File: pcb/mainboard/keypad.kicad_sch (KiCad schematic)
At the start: 20 parts, among them Y100 Crystal

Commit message: - pcb: working on r0p1 sch
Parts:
- removed ARM_JTAG1: Conn_02x05_Odd_Even, Connector_PinHeader_1.27mm:PinHeader_2x05_P1.27mm_Vertical_SMD, symbol Connector_Generic:Conn_02x05_Odd_Even
- removed C112, C113: 470nF, Capacitor_SMD:C_0402_1005Metric, symbol Device:C
- removed C114: 4.7uF, Capacitor_SMD:C_0603_1608Metric, symbol Device:C
- removed C115, C116: 18pF, Capacitor_SMD:C_0402_1005Metric, symbol Device:C
- removed C?: 100nF, symbol Device:C
- removed D100, D101: 1N5819, Diode_SMD:D_SOD-123, symbol Device:D_Schottky
- removed FB?: Ferrite_Bead, symbol Device:Ferrite_Bead
- removed J?: Conn_01x24_MountingPin, symbol Connector_Generic_MountingPin:Conn_01x24_MountingPin
- removed J?: Conn_01x12_MountingPin, symbol Connector_Generic_MountingPin:Conn_01x12_MountingPin
- removed R109: 2.2M, Capacitor_SMD:C_0402_1005Metric, symbol Device:R
- removed R110, R111, R118: 10K, Capacitor_SMD:C_0402_1005Metric, symbol Device:R
- removed R114, R115: 22R, Capacitor_SMD:C_0402_1005Metric, symbol Device:R
- removed U?: GD32VF103C8Tx, Package_QFP:LQFP-48_7x7mm_P0.5mm, symbol MCU_ST_STM32F1:STM32F103C8Tx
- removed Y100: Crystal, Crystal:Crystal_SMD_TXC_9HT11-2Pin_2.0x1.2mm_HandSoldering, symbol Device:Crystal
- added J?: Conn_01x28_MountingPin, symbol Connector_Generic_MountingPin:Conn_01x28_MountingPin
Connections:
- net GND: now also J?.28 (Pin_28), J?.MP (MountPin)
- new net KBD_DET: J?.27 (Pin_27)
- new net KSI0: J?.2 (Pin_2)
- new net KSI1: J?.5 (Pin_5)
- new net KSI2: J?.7 (Pin_7)
- new net KSI3: J?.9 (Pin_9)
- new net KSI4: J?.11 (Pin_11)
- new net KSI5: J?.12 (Pin_12)
- new net KSI6: J?.14 (Pin_14)
- new net KSI7: J?.15 (Pin_15)
- new net KSO0: J?.1 (Pin_1)
- new net KSO1: J?.22 (Pin_22), J?.3 (Pin_3)
- new net KSO10: J?.19 (Pin_19)
- new net KSO11: J?.20 (Pin_20)
- new net KSO12: J?.21 (Pin_21)
- new net KSO13: J?.23 (Pin_23)
- new net KSO14: J?.24 (Pin_24)
- new net KSO15: J?.26 (Pin_26)
- new net KSO2: J?.4 (Pin_4)
- new net KSO3: J?.25 (Pin_25), J?.6 (Pin_6)
- new net KSO4: J?.8 (Pin_8)
- new net KSO5: J?.10 (Pin_10)
- new net KSO6: J?.13 (Pin_13)
- new net KSO7: J?.16 (Pin_16)
- new net KSO8: J?.17 (Pin_17)
- new net KSO9: J?.18 (Pin_18)
- no-connect marks 9 -> 0

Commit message: - pcb: r0p1 sch draft
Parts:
- gave numbers to parts that had none: 1
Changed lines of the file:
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@@
 (kicad_sch (version 20210406) (generator eeschema)
-  (paper "A4")
+  (paper "A3")
   (title_block
     (title "Archer")
@@
   (symbol (lib_id "Connector_Generic_MountingPin:Conn_01x28_MountingPin") (at 160.02 96.52 0) (unit 1)
     (in_bom yes) (on_board yes) (fields_autoplaced)
-    (property "Reference" "J?" (id 0) (at 162.56 99.1869 0)
+    (property "Reference" "J800" (id 0) (at 162.56 99.1869 0)
       (effects (font (size 1.27 1.27)) (justify left))
     )

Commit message: - pcb: start r0p1 layout
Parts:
- J800: footprint (none) -> Connector_FFC-FPC:Molex_200528-0280_1x28-1MP_P1.00mm_Horizontal
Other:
- company: Copyright EI-2030 2021. -> Copyright EI-2030 2021. / Engineer: Wenting Zhang
- title: Archer -> Archer Mainboard
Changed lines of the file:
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@@
   (paper "A3")
   (title_block
-    (title "Archer")
-    (date "2021-04-26")
+    (title "Archer Mainboard")
+    (date "2021-05-05")
     (rev "R0.1 draft")
-    (company "Copyright EI-2030 2021.")
+    (company "Copyright EI-2030 2021. / Engineer: Wenting Zhang")
     (comment 2 "MERCHANTABILITY, SATISFACTORY QUALITY AND FITNESS FOR A PARTICULAR PURPOSE.")
-    (comment 3 "source is distributed WITHOUT ANY EXPRESS OR IMPLIED WARRANTY, INCLUDING OF")
-    (comment 4 "This source describes Open Hardware and is licensed under the CERN-OHL-S v2. This ")
+    (comment 3 "This source is distributed WITHOUT ANY EXPRESS OR IMPLIED WARRANTY, INCLUDING OF")
+    (comment 4 "This source describes Open Hardware and is licensed under the CERN-OHL-S v2.")
   )
   (junction (at 149.86 68.58) (diameter 0.9144) (color 0 0 0 0))
@@
     (stroke (width 0) (type solid) (color 0 0 0 0))
   )
-  (global_label "KSO0" (shape output) (at 147.32 63.5 180) (fields_autoplaced)
+  (global_label "KSO0" (shape input) (at 147.32 63.5 180) (fields_autoplaced)
     (effects (font (size 1.27 1.27)) (justify right))
     (property "Intersheet References" "${INTERSHEET_REFS}" (id 0) (at 139.8874 63.4206 0)
@@
     )
   )
-  (global_label "KSI0" (shape input) (at 147.32 66.04 180) (fields_autoplaced)
+  (global_label "KSI0" (shape output) (at 147.32 66.04 180) (fields_autoplaced)
     (effects (font (size 1.27 1.27)) (justify right))
     (property "Intersheet References" "${INTERSHEET_REFS}" (id 0) (at 140.6131 65.9606 0)
@@
     )
   )
-  (global_label "KSO1" (shape output) (at 147.32 68.58 180) (fields_autoplaced)
+  (global_label "KSO1" (shape input) (at 147.32 68.58 180) (fields_autoplaced)
     (effects (font (size 1.27 1.27)) (justify right))
     (property "Intersheet References" "${INTERSHEET_REFS}" (id 0) (at 139.8874 68.5006 0)
@@
     )
   )
-  (global_label "KSO2" (shape output) (at 147.32 71.12 180) (fields_autoplaced)
+  (global_label "KSO2" (shape input) (at 147.32 71.12 180) (fields_autoplaced)
     (effects (font (size 1.27 1.27)) (justify right))
     (property "Intersheet References" "${INTERSHEET_REFS}" (id 0) (at 139.8874 71.0406 0)
@@
     )
   )
-  (global_label "KSI1" (shape input) (at 147.32 73.66 180) (fields_autoplaced)
+  (global_label "KSI1" (shape output) (at 147.32 73.66 180) (fields_autoplaced)
     (effects (font (size 1.27 1.27)) (justify right))
     (property "Intersheet References" "${INTERSHEET_REFS}" (id 0) (at 140.6131 73.5806 0)
@@
     )
   )
-  (global_label "KSO3" (shape output) (at 147.32 76.2 180) (fields_autoplaced)
+  (global_label "KSO3" (shape input) (at 147.32 76.2 180) (fields_autoplaced)
     (effects (font (size 1.27 1.27)) (justify right))
     (property "Intersheet References" "${INTERSHEET_REFS}" (id 0) (at 139.8874 76.1206 0)
@@
     )
   )
-  (global_label "KSI2" (shape input) (at 147.32 78.74 180) (fields_autoplaced)
+  (global_label "KSI2" (shape output) (at 147.32 78.74 180) (fields_autoplaced)
     (effects (font (size 1.27 1.27)) (justify right))
     (property "Intersheet References" "${INTERSHEET_REFS}" (id 0) (at 140.6131 78.6606 0)
@@
     )
   )
-  (global_label "KSO4" (shape output) (at 147.32 81.28 180) (fields_autoplaced)
+  (global_label "KSO4" (shape input) (at 147.32 81.28 180) (fields_autoplaced)
     (effects (font (size 1.27 1.27)) (justify right))
     (property "Intersheet References" "${INTERSHEET_REFS}" (id 0) (at 139.8874 81.2006 0)
@@
     )
   )
-  (global_label "KSI3" (shape input) (at 147.32 83.82 180) (fields_autoplaced)
+  (global_label "KSI3" (shape output) (at 147.32 83.82 180) (fields_autoplaced)
     (effects (font (size 1.27 1.27)) (justify right))
     (property "Intersheet References" "${INTERSHEET_REFS}" (id 0) (at 140.6131 83.7406 0)
@@
     )
   )
-  (global_label "KSO5" (shape output) (at 147.32 86.36 180) (fields_autoplaced)
+  (global_label "KSO5" (shape input) (at 147.32 86.36 180) (fields_autoplaced)
     (effects (font (size 1.27 1.27)) (justify right))
     (property "Intersheet References" "${INTERSHEET_REFS}" (id 0) (at 139.8874 86.2806 0)
@@
     )
   )
-  (global_label "KSI4" (shape input) (at 147.32 88.9 180) (fields_autoplaced)
+  (global_label "KSI4" (shape output) (at 147.32 88.9 180) (fields_autoplaced)
     (effects (font (size 1.27 1.27)) (justify right))
     (property "Intersheet References" "${INTERSHEET_REFS}" (id 0) (at 140.6131 88.8206 0)
@@
     )
   )
-  (global_label "KSI5" (shape input) (at 147.32 91.44 180) (fields_autoplaced)
+  (global_label "KSI5" (shape output) (at 147.32 91.44 180) (fields_autoplaced)
     (effects (font (size 1.27 1.27)) (justify right))
     (property "Intersheet References" "${INTERSHEET_REFS}" (id 0) (at 140.6131 91.3606 0)
@@
     )
   )
-  (global_label "KSO6" (shape output) (at 147.32 93.98 180) (fields_autoplaced)
+  (global_label "KSO6" (shape input) (at 147.32 93.98 180) (fields_autoplaced)
     (effects (font (size 1.27 1.27)) (justify right))
     (property "Intersheet References" "${INTERSHEET_REFS}" (id 0) (at 139.8874 93.9006 0)
@@
     )
   )
-  (global_label "KSI6" (shape input) (at 147.32 96.52 180) (fields_autoplaced)
+  (global_label "KSI6" (shape output) (at 147.32 96.52 180) (fields_autoplaced)
     (effects (font (size 1.27 1.27)) (justify right))
     (property "Intersheet References" "${INTERSHEET_REFS}" (id 0) (at 140.6131 96.4406 0)
@@
     )
   )
-  (global_label "KSI7" (shape input) (at 147.32 99.06 180) (fields_autoplaced)
+  (global_label "KSI7" (shape output) (at 147.32 99.06 180) (fields_autoplaced)
     (effects (font (size 1.27 1.27)) (justify right))
     (property "Intersheet References" "${INTERSHEET_REFS}" (id 0) (at 140.6131 98.9806 0)
@@
     )
   )
-  (global_label "KSO7" (shape output) (at 147.32 101.6 180) (fields_autoplaced)
+  (global_label "KSO7" (shape input) (at 147.32 101.6 180) (fields_autoplaced)
     (effects (font (size 1.27 1.27)) (justify right))
     (property "Intersheet References" "${INTERSHEET_REFS}" (id 0) (at 139.8874 101.5206 0)
@@
     )
   )
-  (global_label "KSO8" (shape output) (at 147.32 104.14 180) (fields_autoplaced)
+  (global_label "KSO8" (shape input) (at 147.32 104.14 180) (fields_autoplaced)
     (effects (font (size 1.27 1.27)) (justify right))
     (property "Intersheet References" "${INTERSHEET_REFS}" (id 0) (at 139.8874 104.0606 0)
@@
     )
   )
-  (global_label "KSO9" (shape output) (at 147.32 106.68 180) (fields_autoplaced)
+  (global_label "KSO9" (shape input) (at 147.32 106.68 180) (fields_autoplaced)
     (effects (font (size 1.27 1.27)) (justify right))
     (property "Intersheet References" "${INTERSHEET_REFS}" (id 0) (at 139.8874 106.6006 0)
@@
     )
   )
-  (global_label "KSO10" (shape output) (at 147.32 109.22 180) (fields_autoplaced)
+  (global_label "KSO10" (shape input) (at 147.32 109.22 180) (fields_autoplaced)
     (effects (font (size 1.27 1.27)) (justify right))
     (property "Intersheet References" "${INTERSHEET_REFS}" (id 0) (at 139.8874 109.1406 0)
@@
     )
   )
-  (global_label "KSO11" (shape output) (at 147.32 111.76 180) (fields_autoplaced)
+  (global_label "KSO11" (shape input) (at 147.32 111.76 180) (fields_autoplaced)
     (effects (font (size 1.27 1.27)) (justify right))
     (property "Intersheet References" "${INTERSHEET_REFS}" (id 0) (at 139.8874 111.6806 0)
@@
     )
   )
-  (global_label "KSO12" (shape output) (at 147.32 114.3 180) (fields_autoplaced)
+  (global_label "KSO12" (shape input) (at 147.32 114.3 180) (fields_autoplaced)
     (effects (font (size 1.27 1.27)) (justify right))
     (property "Intersheet References" "${INTERSHEET_REFS}" (id 0) (at 139.8874 114.2206 0)
@@
     )
   )
-  (global_label "KSO13" (shape output) (at 147.32 119.38 180) (fields_autoplaced)
+  (global_label "KSO13" (shape input) (at 147.32 119.38 180) (fields_autoplaced)
     (effects (font (size 1.27 1.27)) (justify right))
     (property "Intersheet References" "${INTERSHEET_REFS}" (id 0) (at 139.8874 119.3006 0)
@@
     )
   )
-  (global_label "KSO14" (shape output) (at 147.32 121.92 180) (fields_autoplaced)
+  (global_label "KSO14" (shape input) (at 147.32 121.92 180) (fields_autoplaced)
     (effects (font (size 1.27 1.27)) (justify right))
     (property "Intersheet References" "${INTERSHEET_REFS}" (id 0) (at 139.8874 121.8406 0)
@@
     )
   )
-  (global_label "KSO15" (shape output) (at 147.32 127 180) (fields_autoplaced)
+  (global_label "KSO15" (shape input) (at 147.32 127 180) (fields_autoplaced)
     (effects (font (size 1.27 1.27)) (justify right))
     (property "Intersheet References" "${INTERSHEET_REFS}" (id 0) (at 139.8874 126.9206 0)
@@
   (symbol (lib_id "power:GND") (at 160.02 139.7 0) (unit 1)
     (in_bom yes) (on_board yes) (fields_autoplaced)
-    (property "Reference" "#PWR?" (id 0) (at 160.02 146.05 0)
+    (property "Reference" "#PWR084" (id 0) (at 160.02 146.05 0)
       (effects (font (size 1.27 1.27)) hide)
     )
@@
       (effects (font (size 1.27 1.27)) (justify left))
     )
-    (property "Footprint" "" (id 2) (at 160.02 96.52 0)
-      (effects (font (size 1.27 1.27)) hide)
-    )
+    (property "Footprint" "Connector_FFC-FPC:Molex_200528-0280_1x28-1MP_P1.00mm_Horizontal" (id 2) (at 160.02 96.52 0)
+      (effects (font (size 1.27 1.27)) hide)
+    )

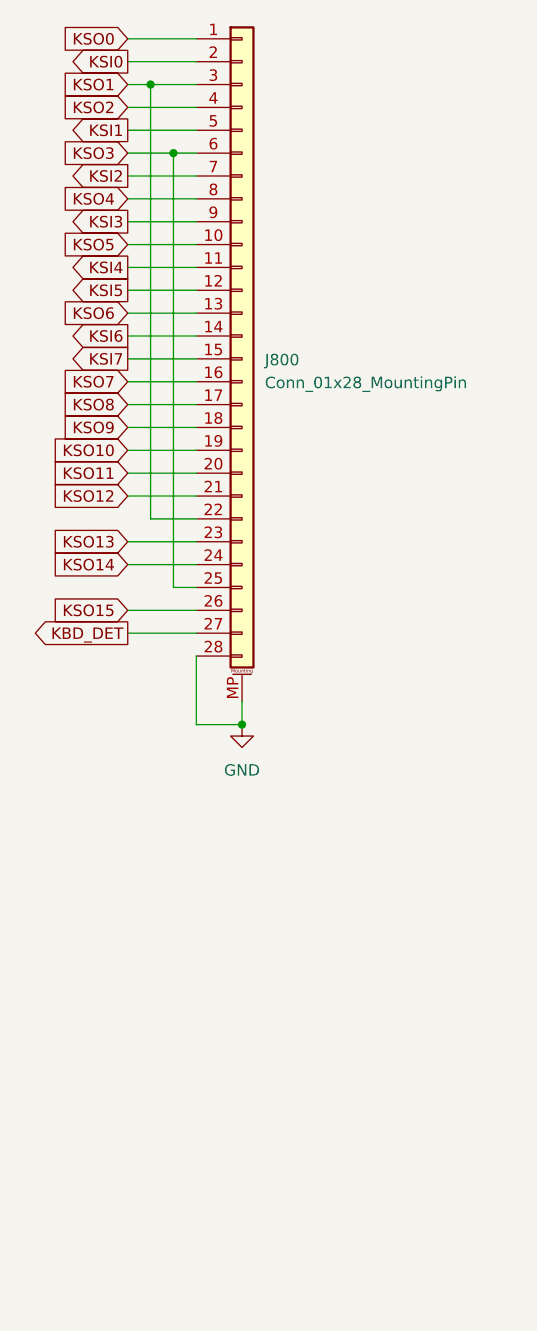
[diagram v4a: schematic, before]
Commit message: - pcb: components placed
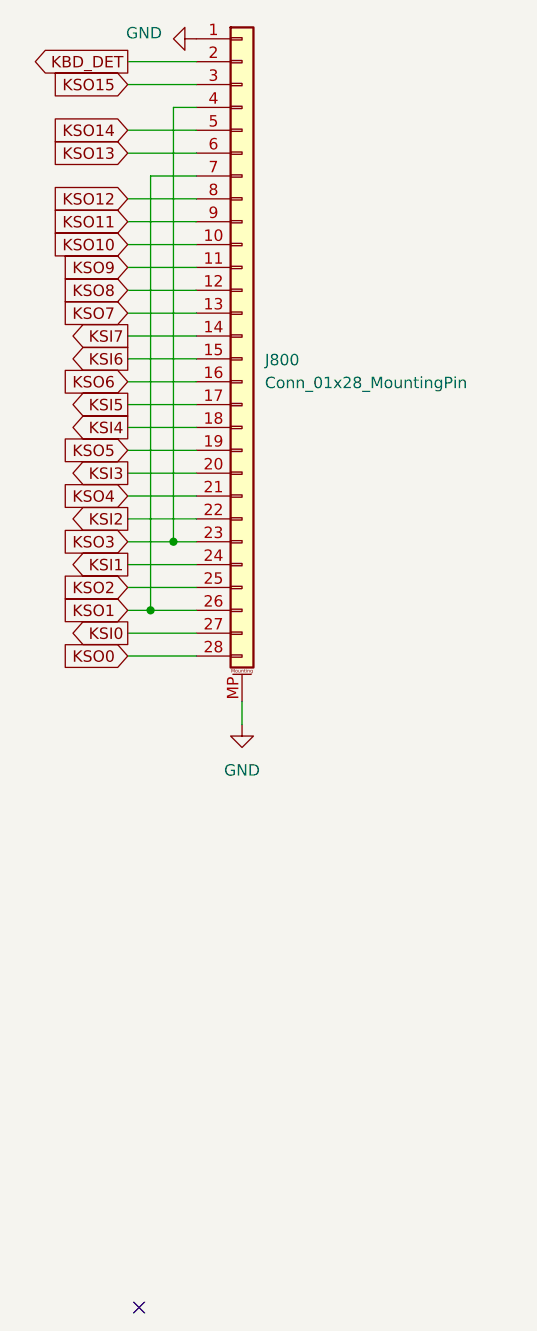
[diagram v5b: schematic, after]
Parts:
- J800: footprint Connector_FFC-FPC:Molex_200528-0280_1x28-1MP_P1.00mm_Horizontal -> Connector_FFC-FPC:TE_2-84953-8_1x28-1MP_P1.0mm_Horizontal
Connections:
- net GND: now also J800.1 (Pin_1); no longer J800.28 (Pin_28)
- net KBD_DET: now also J800.2 (Pin_2); no longer J800.27 (Pin_27)
- net KSI0: now also J800.27 (Pin_27); no longer J800.2 (Pin_2)
- net KSI1: now also J800.24 (Pin_24); no longer J800.5 (Pin_5)
- net KSI2: now also J800.22 (Pin_22); no longer J800.7 (Pin_7)
- net KSI3: now also J800.20 (Pin_20); no longer J800.9 (Pin_9)
- net KSI4: now also J800.18 (Pin_18); no longer J800.11 (Pin_11)
- net KSI5: now also J800.17 (Pin_17); no longer J800.12 (Pin_12)
- net KSI6: now also J800.15 (Pin_15); no longer J800.14 (Pin_14)
- net KSI7: now also J800.14 (Pin_14); no longer J800.15 (Pin_15)
- net KSO0: now also J800.28 (Pin_28); no longer J800.1 (Pin_1)
- net KSO1: now also J800.26 (Pin_26), J800.7 (Pin_7); no longer J800.22 (Pin_22), J800.3 (Pin_3)
- net KSO10: now also J800.10 (Pin_10); no longer J800.19 (Pin_19)
- net KSO11: now also J800.9 (Pin_9); no longer J800.20 (Pin_20)
- net KSO12: now also J800.8 (Pin_8); no longer J800.21 (Pin_21)
- net KSO13: now also J800.6 (Pin_6); no longer J800.23 (Pin_23)
- net KSO14: now also J800.5 (Pin_5); no longer J800.24 (Pin_24)
- net KSO15: now also J800.3 (Pin_3); no longer J800.26 (Pin_26)
- net KSO2: now also J800.25 (Pin_25); no longer J800.4 (Pin_4)
- net KSO3: now also J800.23 (Pin_23), J800.4 (Pin_4); no longer J800.25 (Pin_25), J800.6 (Pin_6)
- net KSO4: now also J800.21 (Pin_21); no longer J800.8 (Pin_8)
- net KSO5: now also J800.19 (Pin_19); no longer J800.10 (Pin_10)
- net KSO6: now also J800.16 (Pin_16); no longer J800.13 (Pin_13)
- net KSO7: now also J800.13 (Pin_13); no longer J800.16 (Pin_16)
- net KSO8: now also J800.12 (Pin_12); no longer J800.17 (Pin_17)
- net KSO9: now also J800.11 (Pin_11); no longer J800.18 (Pin_18)
- no-connect marks 0 -> 1

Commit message: - pcb: finishing layout r0p1
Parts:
- added C800: 100nF, Capacitor_SMD:C_0402_1005Metric, symbol Device:C
- added R800: 1K, Resistor_SMD:R_0402_1005Metric, symbol Device:R
- added SW800: EVQPUJ02K, Button_Switch_SMD:Panasonic_EVQPUJ_EVQPUA, symbol Switch:SW_Push
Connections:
- net GND: now also C800.1, SW800.2
- new net: R800.1, SW800.1
- new net ONOFF: C800.2, R800.2
- no-connect marks 1 -> 0
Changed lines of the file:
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@@
     (comment 4 "This source describes Open Hardware and is licensed under the CERN-OHL-S v2.")
   )
+  (junction (at 132.08 162.56) (diameter 0.9144) (color 0 0 0 0))
   (junction (at 149.86 127) (diameter 0.9144) (color 0 0 0 0))
   (junction (at 152.4 119.38) (diameter 0.9144) (color 0 0 0 0))
-  (no_connect (at 148.59 204.47))
+  (wire (pts (xy 129.54 162.56) (xy 132.08 162.56))
+    (stroke (width 0) (type solid) (color 0 0 0 0))
+  )
+  (wire (pts (xy 132.08 162.56) (xy 132.08 165.1))
+    (stroke (width 0) (type solid) (color 0 0 0 0))
+  )
+  (wire (pts (xy 132.08 162.56) (xy 134.62 162.56))
+    (stroke (width 0) (type solid) (color 0 0 0 0))
+  )
+  (wire (pts (xy 132.08 172.72) (xy 132.08 175.26))
+    (stroke (width 0) (type solid) (color 0 0 0 0))
+  )
+  (wire (pts (xy 142.24 162.56) (xy 147.32 162.56))
+    (stroke (width 0) (type solid) (color 0 0 0 0))
+  )
   (wire (pts (xy 147.32 66.04) (xy 154.94 66.04))
     (stroke (width 0) (type solid) (color 0 0 0 0))
@@
     (stroke (width 0) (type solid) (color 0 0 0 0))
   )
+  (global_label "ONOFF" (shape output) (at 129.54 162.56 180) (fields_autoplaced)
+    (effects (font (size 1.27 1.27)) (justify right))
+    (property "Intersheet References" "${INTERSHEET_REFS}" (id 0) (at 120.9583 162.4806 0)
+      (effects (font (size 1.27 1.27)) (justify right) hide)
+    )
+  )
   (global_label "KBD_DET" (shape output) (at 147.32 66.04 180) (fields_autoplaced)
     (effects (font (size 1.27 1.27)) (justify right))
@@
       (effects (font (size 1.27 1.27)) (justify right) hide)
     )
+  )
+  (symbol (lib_id "power:GND") (at 132.08 175.26 0) (unit 1)
+    (in_bom yes) (on_board yes) (fields_autoplaced)
+    (property "Reference" "#PWR0165" (id 0) (at 132.08 181.61 0)
+      (effects (font (size 1.27 1.27)) hide)
+    )
+    (property "Value" "GND" (id 1) (at 132.08 180.34 0))
+    (property "Footprint" "" (id 2) (at 132.08 175.26 0)
+      (effects (font (size 1.27 1.27)) hide)
+    )
+    (property "Datasheet" "" (id 3) (at 132.08 175.26 0)
+      (effects (font (size 1.27 1.27)) hide)
+    )
+    (pin "1")
   )
   (symbol (lib_id "power:GND") (at 154.94 63.5 270) (unit 1)
@@
     )
     (property "Datasheet" "" (id 3) (at 154.94 63.5 0)
+      (effects (font (size 1.27 1.27)) hide)
+    )
+    (pin "1")
+  )
+  (symbol (lib_id "power:GND") (at 157.48 162.56 90) (unit 1)
+    (in_bom yes) (on_board yes)
+    (property "Reference" "#PWR0164" (id 0) (at 163.83 162.56 0)
+      (effects (font (size 1.27 1.27)) hide)
+    )
+    (property "Value" "GND" (id 1) (at 163.83 162.56 90))
+    (property "Footprint" "" (id 2) (at 157.48 162.56 0)
+      (effects (font (size 1.27 1.27)) hide)
+    )
+    (property "Datasheet" "" (id 3) (at 157.48 162.56 0)
       (effects (font (size 1.27 1.27)) hide)
     )
@@
     (pin "1")
   )
+  (symbol (lib_id "Device:R") (at 138.43 162.56 270) (unit 1)
+    (in_bom yes) (on_board yes)
+    (property "Reference" "R800" (id 0) (at 133.35 161.29 90))
+    (property "Value" "1K" (id 1) (at 143.51 161.29 90))
+    (property "Footprint" "Resistor_SMD:R_0402_1005Metric" (id 2) (at 138.43 160.782 90)
+      (effects (font (size 1.27 1.27)) hide)
+    )
+    (property "Datasheet" "~" (id 3) (at 138.43 162.56 0)
+      (effects (font (size 1.27 1.27)) hide)
+    )
+    (pin "1")
+    (pin "2")
+  )
+  (symbol (lib_id "Device:C") (at 132.08 168.91 180) (unit 1)
+    (in_bom yes) (on_board yes)
+    (property "Reference" "C800" (id 0) (at 137.16 167.64 0))
+    (property "Value" "100nF" (id 1) (at 137.16 170.18 0))
+    (property "Footprint" "Capacitor_SMD:C_0402_1005Metric" (id 2) (at 131.1148 165.1 0)
+      (effects (font (size 1.27 1.27)) hide)
+    )
+    (property "Datasheet" "~" (id 3) (at 132.08 168.91 0)
+      (effects (font (size 1.27 1.27)) hide)
+    )
+    (pin "1")
+    (pin "2")
+  )
+  (symbol (lib_id "Switch:SW_Push") (at 152.4 162.56 0) (unit 1)
+    (in_bom yes) (on_board yes)
+    (property "Reference" "SW800" (id 0) (at 152.4 154.94 0))
+    (property "Value" "EVQPUJ02K" (id 1) (at 152.4 157.48 0))
+    (property "Footprint" "Button_Switch_SMD:Panasonic_EVQPUJ_EVQPUA" (id 2) (at 152.4 157.48 0)
+      (effects (font (size 1.27 1.27)) hide)
+    )
+    (property "Datasheet" "~" (id 3) (at 152.4 157.48 0)
+      (effects (font (size 1.27 1.27)) hide)
+    )
+    (pin "1")
+    (pin "2")
+  )
   (symbol (lib_id "Connector_Generic_MountingPin:Conn_01x28_MountingPin") (at 160.02 96.52 0) (unit 1)
